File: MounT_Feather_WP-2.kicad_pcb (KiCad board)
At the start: 2 copper layers, 50.8 x 22.9 mm, 11 parts, among them J1 Adafruit_Feather, J2 DE9_Female, U1 MAX3232

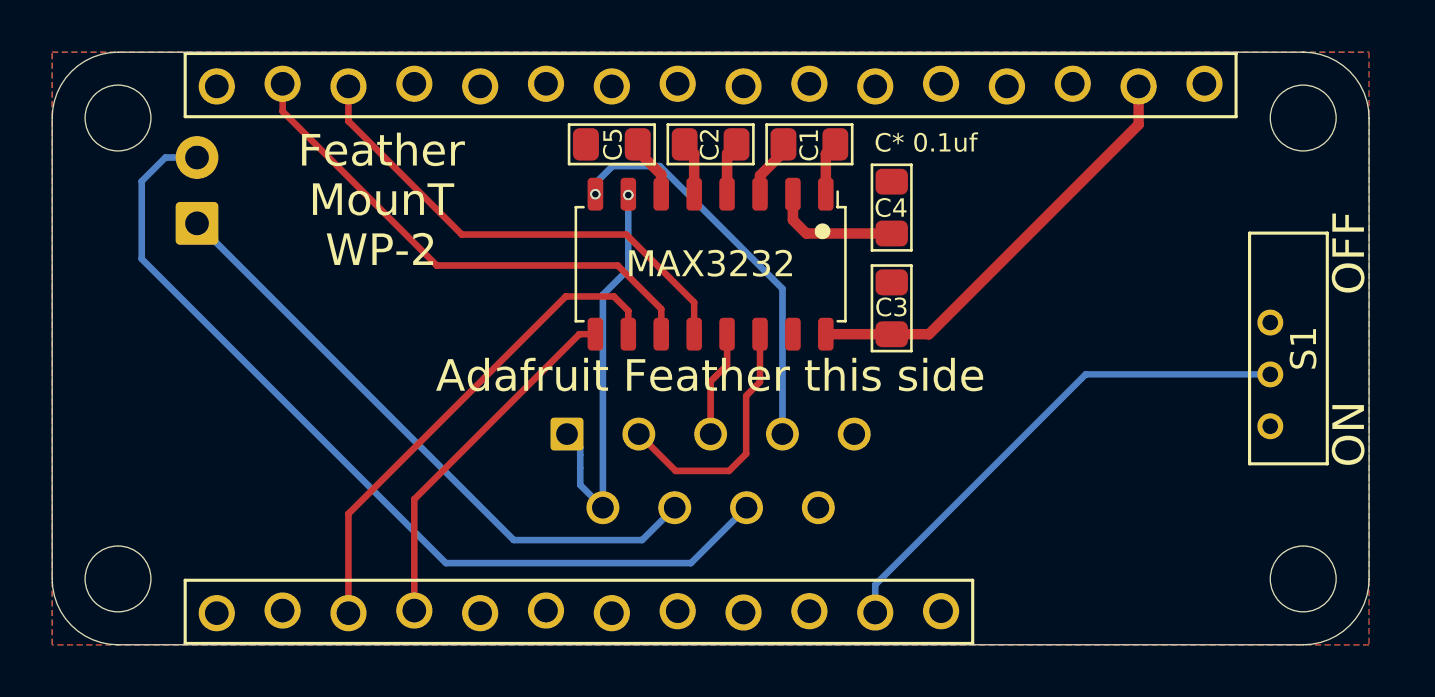
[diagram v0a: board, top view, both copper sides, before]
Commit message: WP2 & Z88, move DE9 shell away from pins. Increase solder pads in S1.
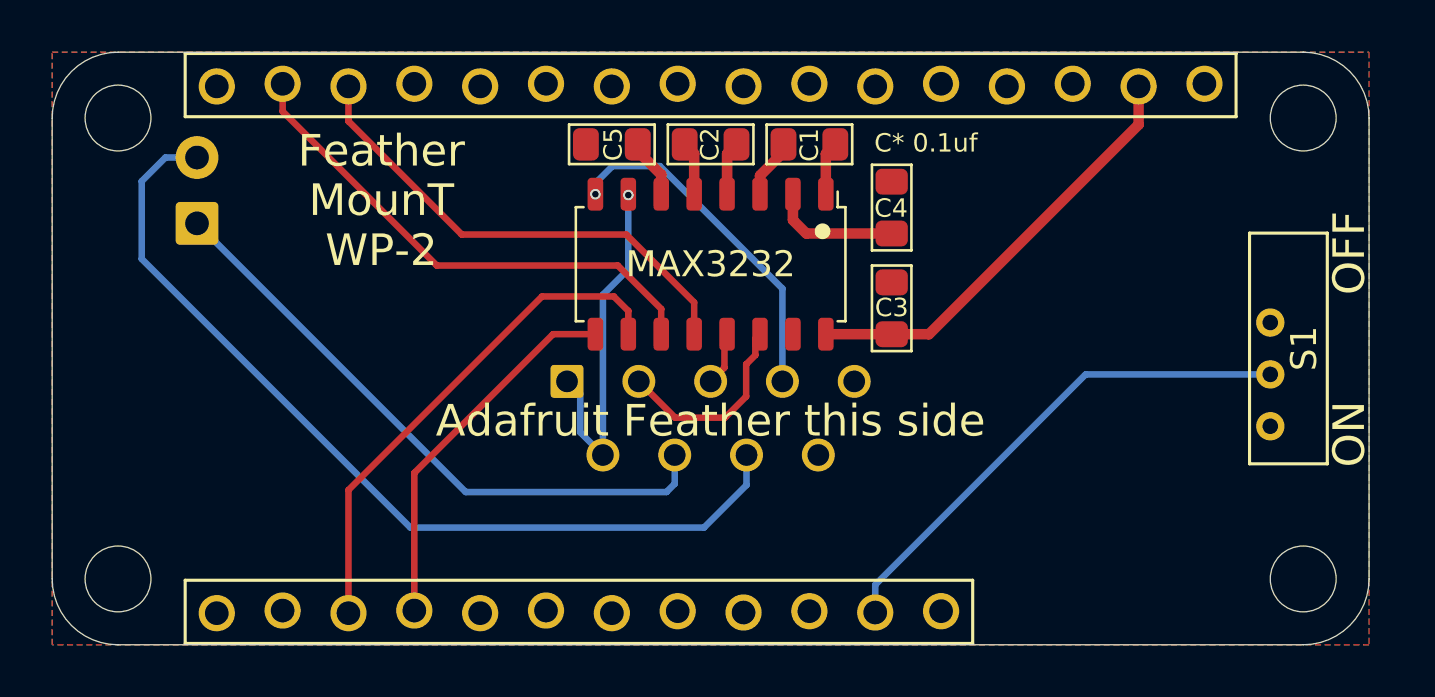
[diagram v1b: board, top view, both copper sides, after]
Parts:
- moved NT1 2.39 mm to (142.3, 98.5)
- moved J2 2.03 mm to (141.8, 97.8)
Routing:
- net /RX_232: track 9.84 -> 7.68 mm
- net /TX_232: track 4.12 -> 2.08 mm
- net /DTR_232: track 15.5 -> 13.5 mm
- net /DSR_232: track 14.4 -> 12.7 mm
- net /DCD_232: track 1.02 -> 0.00 mm
- net /DSR_TTL: track 13.8 -> 14.4 mm
- net /DTR_TTL: track 19.3 -> 19.9 mm

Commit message: use 6mil stagger, 4mil wasn't good enough
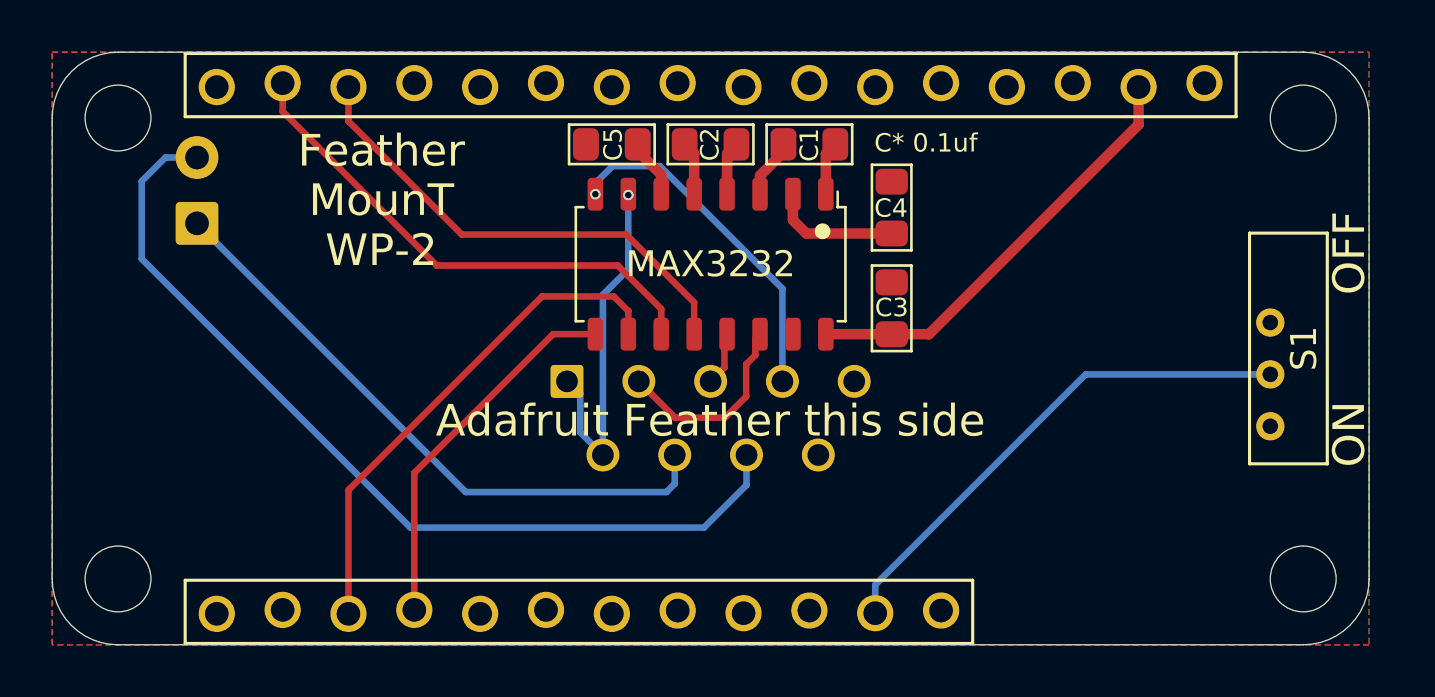
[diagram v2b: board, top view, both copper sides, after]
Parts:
- J1: footprint 0_LOCAL:Adafruit_Feather_stagger_4mil -> 0_LOCAL:Adafruit_Feather_stagger_6mil
